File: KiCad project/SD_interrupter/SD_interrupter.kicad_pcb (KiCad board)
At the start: 2 copper layers, 83.8 x 86.4 mm, 36 parts, among them J1 Micro_SD_Card_Det, J2 AVR-ISP-6, J3 DIN-5, SW1 BL_SW, SW2 MAIN_SW, SW3 UP_SW, SW4 DN_SW, SW5 OK_SW, U1 LM7805_TO220, U2 4050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

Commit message: minor changes
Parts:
- added J4: Jack-DC, Connector_BarrelJack:BarrelJack_Horizontal, F.Cu at (90.7, 86.9)
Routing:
- net VCC: track 29.1 -> 95.3 mm
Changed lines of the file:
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@@
   (net 23 "unconnected-(J1-Pad1)")
   (net 24 "Net-(J1-Pad2)")
-  (net 25 "Net-(U2-Pad4)")
+  (net 25 "Net-(J1-Pad3)")
   (net 26 "Net-(J1-Pad5)")
   (net 27 "/DO")
@@
       (net 31 "/CLK") (pintype "input"))
     (pad "4" thru_hole oval (at 0 7.62 180) (size 1.6 1.6) (drill 0.8) (layers *.Cu *.Mask)
-      (net 25 "Net-(U2-Pad4)") (pintype "output"))
+      (net 25 "Net-(J1-Pad3)") (pintype "output"))
     (pad "5" thru_hole oval (at 0 10.16 180) (size 1.6 1.6) (drill 0.8) (layers *.Cu *.Mask)
       (net 32 "/DI") (pintype "input"))
@@
     (fp_circle (center 3.25 2.25) (end 1.25 2.5) (layer "F.Fab") (width 0.1) (fill none))
     (pad "1" thru_hole circle (at 0 0 90) (size 2 2) (drill 1.1) (layers *.Cu *.Mask)
-      (net 3 "GND") (pinfunction "2") (pintype "passive"))
+      (net 3 "GND") (pinfunction "1") (pintype "passive"))
     (pad "1" thru_hole circle (at 6.5 0 90) (size 2 2) (drill 1.1) (layers *.Cu *.Mask)
-      (net 3 "GND") (pinfunction "2") (pintype "passive"))
+      (net 3 "GND") (pinfunction "1") (pintype "passive"))
     (pad "2" thru_hole circle (at 6.5 4.5 90) (size 2 2) (drill 1.1) (layers *.Cu *.Mask)
       (net 38 "/UP") (pinfunction "A") (pintype "passive"))
@@
       (net 33 "/RESET") (pintype "passive"))
     (model "${KICAD6_3DMODEL_DIR}/Resistor_THT.3dshapes/R_Axial_DIN0204_L3.6mm_D1.6mm_P7.62mm_Horizontal.wrl"
+      (offset (xyz 0 0 0))
+      (scale (xyz 1 1 1))
+      (rotate (xyz 0 0 0))
+    )
+  )
+  (footprint "Connector_BarrelJack:BarrelJack_Horizontal" (layer "F.Cu")
+    (at 90.678 86.868 180)
+    (descr "DC Barrel Jack")
+    (tags "Power Jack")
+    (property "Sheetfile" "SD_interrupter.kicad_sch")
+    (property "Sheetname" "")
+    (attr through_hole)
+    (fp_text reference "J4" (at -8.45 5.75) (layer "F.SilkS")
+      (effects (font (size 1 1) (thickness 0.15)))
+    )
+    (fp_text value "Jack-DC" (at -6.2 -5.5) (layer "F.Fab")
+      (effects (font (size 1 1) (thickness 0.15)))
+    )
+    (fp_text user "${REFERENCE}" (at -3 -2.95) (layer "F.Fab")
+      (effects (font (size 1 1) (thickness 0.15)))
+    )
+    (fp_line (start -13.8 -4.6) (end 0.9 -4.6) (layer "F.SilkS") (width 0.12))
+    (fp_line (start -13.8 4.6) (end -13.8 -4.6) (layer "F.SilkS") (width 0.12))
+    (fp_line (start 0.9 1.9) (end 0.9 4.6) (layer "F.SilkS") (width 0.12))
+    (fp_line (start 0.05 -4.8) (end 1.1 -4.8) (layer "F.SilkS") (width 0.12))
+    (fp_line (start -5 4.6) (end -13.8 4.6) (layer "F.SilkS") (width 0.12))
+    (fp_line (start 0.9 -4.6) (end 0.9 -2) (layer "F.SilkS") (width 0.12))
+    (fp_line (start 0.9 4.6) (end -1 4.6) (layer "F.SilkS") (width 0.12))
+    (fp_line (start 1.1 -3.75) (end 1.1 -4.8) (layer "F.SilkS") (width 0.12))
+    (fp_line (start 2 -2) (end 2 2) (layer "F.CrtYd") (width 0.05))
+    (fp_line (start 2 2) (end 1 2) (layer "F.CrtYd") (width 0.05))
+    (fp_line (start -14 4.75) (end -14 -4.75) (layer "F.CrtYd") (width 0.05))
+    (fp_line (start 1 4.75) (end -1 4.75) (layer "F.CrtYd") (width 0.05))
+    (fp_line (start 1 2) (end 1 4.75) (layer "F.CrtYd") (width 0.05))
+    (fp_line (start 1 -4.5) (end 1 -2) (layer "F.CrtYd") (width 0.05))
+    (fp_line (start 1 -4.75) (end -14 -4.75) (layer "F.CrtYd") (width 0.05))
+    (fp_line (start 1 -2) (end 2 -2) (layer "F.CrtYd") (width 0.05))
+    (fp_line (start -1 6.75) (end -5 6.75) (layer "F.CrtYd") (width 0.05))
+    (fp_line (start -5 6.75) (end -5 4.75) (layer "F.CrtYd") (width 0.05))
+    (fp_line (start -1 4.75) (end -1 6.75) (layer "F.CrtYd") (width 0.05))
+    (fp_line (start 1 -4.5) (end 1 -4.75) (layer "F.CrtYd") (width 0.05))
+    (fp_line (start -5 4.75) (end -14 4.75) (layer "F.CrtYd") (width 0.05))
+    (fp_line (start -13.7 4.5) (end 0.8 4.5) (layer "F.Fab") (width 0.1))
+    (fp_line (start 0.8 4.5) (end 0.8 -3.75) (layer "F.Fab") (width 0.1))
+    (fp_line (start 0 -4.5) (end -13.7 -4.5) (layer "F.Fab") (width 0.1))
+    (fp_line (start -10.2 -4.5) (end -10.2 4.5) (layer "F.Fab") (width 0.1))
+    (fp_line (start -13.7 -4.5) (end -13.7 4.5) (layer "F.Fab") (width 0.1))
+    (fp_line (start -0.003213 -4.505425) (end 0.8 -3.75) (layer "F.Fab") (width 0.1))
+    (pad "1" thru_hole rect (at 0 0 180) (size 3.5 3.5) (drill oval 1 3) (layers *.Cu *.Mask)
+      (net 2 "VCC") (pintype "passive"))
+    (pad "2" thru_hole roundrect (at -6 0 180) (size 3 3.5) (drill oval 1 3) (layers *.Cu *.Mask) (roundrect_rratio 0.25)
+      (net 3 "GND") (pintype "passive"))
+    (pad "3" thru_hole roundrect (at -3 4.7 180) (size 3.5 3.5) (drill oval 3 1) (layers *.Cu *.Mask) (roundrect_rratio 0.25))
+    (model "${KICAD6_3DMODEL_DIR}/Connector_BarrelJack.3dshapes/BarrelJack_Horizontal.wrl"
       (offset (xyz 0 0 0))
       (scale (xyz 1 1 1))
@@
     (fp_circle (center 3.25 2.25) (end 1.25 2.5) (layer "F.Fab") (width 0.1) (fill none))
     (pad "1" thru_hole circle (at 6.5 0 90) (size 2 2) (drill 1.1) (layers *.Cu *.Mask)
-      (net 3 "GND") (pinfunction "1") (pintype "passive"))
+      (net 3 "GND") (pinfunction "2") (pintype "passive"))
     (pad "1" thru_hole circle (at 0 0 90) (size 2 2) (drill 1.1) (layers *.Cu *.Mask)
-      (net 3 "GND") (pinfunction "1") (pintype "passive"))
+      (net 3 "GND") (pinfunction "2") (pintype "passive"))
     (pad "2" thru_hole circle (at 0 4.5 90) (size 2 2) (drill 1.1) (layers *.Cu *.Mask)
       (net 39 "/DN") (pinfunction "A") (pintype "passive"))
@@
       (net 24 "Net-(J1-Pad2)") (pinfunction "DAT3/CD") (pintype "bidirectional"))
     (pad "3" smd rect (at 0.575 -7.725 90) (size 0.7 1.2) (layers "F.Cu" "F.Paste" "F.Mask")
-      (net 25 "Net-(U2-Pad4)") (pinfunction "CMD") (pintype "input"))
+      (net 25 "Net-(J1-Pad3)") (pinfunction "CMD") (pintype "input"))
     (pad "4" smd rect (at -0.525 -7.725 90) (size 0.7 1.2) (layers "F.Cu" "F.Paste" "F.Mask")
       (net 6 "+3.3V") (pinfunction "VDD") (pintype "power_in"))
@@
     (fp_circle (center 3.25 2.25) (end 1.25 2.5) (layer "F.Fab") (width 0.1) (fill none))
     (pad "1" thru_hole circle (at 0 0 90) (size 2 2) (drill 1.1) (layers *.Cu *.Mask)
-      (net 3 "GND") (pinfunction "1") (pintype "passive"))
+      (net 3 "GND") (pinfunction "2") (pintype "passive"))
     (pad "1" thru_hole circle (at 6.5 0 90) (size 2 2) (drill 1.1) (layers *.Cu *.Mask)
-      (net 3 "GND") (pinfunction "1") (pintype "passive"))
+      (net 3 "GND") (pinfunction "2") (pintype "passive"))
     (pad "2" thru_hole circle (at 0 4.5 90) (size 2 2) (drill 1.1) (layers *.Cu *.Mask)
       (net 40 "/OK") (pinfunction "A") (pintype "passive"))
@@
     (fp_line (start 68 28) (end -5 28) (layer "F.SilkS") (width 0.12))
     (fp_line (start -8.14 -2.64) (end -8.14 33.64) (layer "F.SilkS") (width 0.12))
-    (fp_arc (start 64.20104 22.49932) (mid 64.054473 22.853115) (end 63.70066 22.9997) (layer "F.SilkS") (width 0.12))
+    (fp_arc (start 64.20104 22.49932) (mid 64.054479 22.85315) (end 63.70066 22.9997) (layer "F.SilkS") (width 0.12))
     (fp_arc (start 0.20066 22.9997) (mid -0.153162 22.853142) (end -0.29972 22.49932) (layer "F.SilkS") (width 0.12))
     (fp_arc (start 63.7 8) (mid 64.053553 8.146447) (end 64.2 8.5) (layer "F.SilkS") (width 0.12))
@@
   (segment (start 48.561315 106.981315) (end 50.165 108.585) (width 0.635) (layer "B.Cu") (net 1))
   (segment (start 30.1445 69.5125) (end 30.1445 49.5755) (width 0.635) (layer "B.Cu") (net 2))
+  (segment (start 71.72907 86.868) (end 69.26357 84.4025) (width 0.635) (layer "B.Cu") (net 2))
+  (segment (start 90.678 86.868) (end 71.72907 86.868) (width 0.635) (layer "B.Cu") (net 2))
   (segment (start 31.247 70.615) (end 30.1445 69.5125) (width 0.635) (layer "B.Cu") (net 2))
   (segment (start 30.1445 49.5755) (end 24.765 44.196) (width 0.635) (layer "B.Cu") (net 2))
+  (segment (start 45.0345 84.4025) (end 31.247 70.615) (width 0.635) (layer "B.Cu") (net 2))
+  (segment (start 69.26357 84.4025) (end 45.0345 84.4025) (width 0.635) (layer "B.Cu") (net 2))
   (segment (start 72.39 31.75) (end 72.39 31.83) (width 0.635) (layer "F.Cu") (net 3))
   (segment (start 72.39 31.83) (end 76.12 35.56) (width 0.635) (layer "F.Cu") (net 3))

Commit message: minor changes
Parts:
- added J5: VCC, Connector_PinSocket_2.54mm:PinSocket_1x02_P2.54mm_Vertical, F.Cu at (25.7, 66.0)
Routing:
- net VCC: track 95.3 -> 102.8 mm
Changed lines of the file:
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@@
       (net 3 "GND") (pinfunction "1") (pintype "passive"))
     (pad "2" thru_hole circle (at 6.5 4.5 90) (size 2 2) (drill 1.1) (layers *.Cu *.Mask)
-      (net 38 "/UP") (pinfunction "A") (pintype "passive"))
+      (net 38 "/UP") (pinfunction "K") (pintype "passive"))
     (pad "2" thru_hole circle (at 0 4.5 90) (size 2 2) (drill 1.1) (layers *.Cu *.Mask)
-      (net 38 "/UP") (pinfunction "A") (pintype "passive"))
+      (net 38 "/UP") (pinfunction "K") (pintype "passive"))
     (model "${KICAD6_3DMODEL_DIR}/Button_Switch_THT.3dshapes/SW_PUSH_6mm_H7.3mm.wrl"
       (offset (xyz 0 0 0))
@@
       (net 5 "+5V") (pinfunction "IN") (pintype "power_in"))
     (model "${KICAD6_3DMODEL_DIR}/Package_TO_SOT_THT.3dshapes/TO-92.wrl"
+      (offset (xyz 0 0 0))
+      (scale (xyz 1 1 1))
+      (rotate (xyz 0 0 0))
+    )
+  )
+  (footprint "Connector_PinSocket_2.54mm:PinSocket_1x02_P2.54mm_Vertical" (layer "F.Cu")
+    (at 25.654 66.04 180)
+    (descr "Through hole straight socket strip, 1x02, 2.54mm pitch, single row (from Kicad 4.0.7), script generated")
+    (tags "Through hole socket strip THT 1x02 2.54mm single row")
+    (property "Sheetfile" "SD_interrupter.kicad_sch")
+    (property "Sheetname" "")
+    (attr through_hole)
+    (fp_text reference "J5" (at 0 -2.77) (layer "F.SilkS")
+      (effects (font (size 1 1) (thickness 0.15)))
+    )
+    (fp_text value "VCC" (at 0 5.31) (layer "F.Fab")
+      (effects (font (size 1 1) (thickness 0.15)))
+    )
+    (fp_text user "${REFERENCE}" (at 0 1.27 90) (layer "F.Fab")
+      (effects (font (size 1 1) (thickness 0.15)))
+    )
+    (fp_line (start -1.33 3.87) (end 1.33 3.87) (layer "F.SilkS") (width 0.12))
+    (fp_line (start 0 -1.33) (end 1.33 -1.33) (layer "F.SilkS") (width 0.12))
+    (fp_line (start 1.33 1.27) (end 1.33 3.87) (layer "F.SilkS") (width 0.12))
+    (fp_line (start -1.33 1.27) (end -1.33 3.87) (layer "F.SilkS") (width 0.12))
+    (fp_line (start -1.33 1.27) (end 1.33 1.27) (layer "F.SilkS") (width 0.12))
+    (fp_line (start 1.33 -1.33) (end 1.33 0) (layer "F.SilkS") (width 0.12))
+    (fp_line (start 1.75 -1.8) (end 1.75 4.3) (layer "F.CrtYd") (width 0.05))
+    (fp_line (start -1.8 -1.8) (end 1.75 -1.8) (layer "F.CrtYd") (width 0.05))
+    (fp_line (start 1.75 4.3) (end -1.8 4.3) (layer "F.CrtYd") (width 0.05))
+    (fp_line (start -1.8 4.3) (end -1.8 -1.8) (layer "F.CrtYd") (width 0.05))
+    (fp_line (start -1.27 3.81) (end -1.27 -1.27) (layer "F.Fab") (width 0.1))
+    (fp_line (start -1.27 -1.27) (end 0.635 -1.27) (layer "F.Fab") (width 0.1))
+    (fp_line (start 0.635 -1.27) (end 1.27 -0.635) (layer "F.Fab") (width 0.1))
+    (fp_line (start 1.27 -0.635) (end 1.27 3.81) (layer "F.Fab") (width 0.1))
+    (fp_line (start 1.27 3.81) (end -1.27 3.81) (layer "F.Fab") (width 0.1))
+    (pad "1" thru_hole rect (at 0 0 180) (size 1.7 1.7) (drill 1) (layers *.Cu *.Mask)
+      (net 2 "VCC") (pinfunction "Pin_1") (pintype "passive"))
+    (pad "2" thru_hole oval (at 0 2.54 180) (size 1.7 1.7) (drill 1) (layers *.Cu *.Mask)
+      (net 3 "GND") (pinfunction "Pin_2") (pintype "passive"))
+    (model "${KICAD6_3DMODEL_DIR}/Connector_PinSocket_2.54mm.3dshapes/PinSocket_1x02_P2.54mm_Vertical.wrl"
       (offset (xyz 0 0 0))
       (scale (xyz 1 1 1))
@@
       (net 3 "GND") (pinfunction "2") (pintype "passive"))
     (pad "2" thru_hole circle (at 0 4.5 90) (size 2 2) (drill 1.1) (layers *.Cu *.Mask)
-      (net 39 "/DN") (pinfunction "A") (pintype "passive"))
+      (net 39 "/DN") (pinfunction "K") (pintype "passive"))
     (pad "2" thru_hole circle (at 6.5 4.5 90) (size 2 2) (drill 1.1) (layers *.Cu *.Mask)
-      (net 39 "/DN") (pinfunction "A") (pintype "passive"))
+      (net 39 "/DN") (pinfunction "K") (pintype "passive"))
     (model "${KICAD6_3DMODEL_DIR}/Button_Switch_THT.3dshapes/SW_PUSH_6mm_H7.3mm.wrl"
       (offset (xyz 0 0 0))
@@
     (fp_circle (center 3.25 2.25) (end 1.25 2.5) (layer "F.Fab") (width 0.1) (fill none))
     (pad "1" thru_hole circle (at 0 0 90) (size 2 2) (drill 1.1) (layers *.Cu *.Mask)
-      (net 3 "GND") (pinfunction "2") (pintype "passive"))
+      (net 3 "GND") (pinfunction "1") (pintype "passive"))
     (pad "1" thru_hole circle (at 6.5 0 90) (size 2 2) (drill 1.1) (layers *.Cu *.Mask)
-      (net 3 "GND") (pinfunction "2") (pintype "passive"))
+      (net 3 "GND") (pinfunction "1") (pintype "passive"))
     (pad "2" thru_hole circle (at 0 4.5 90) (size 2 2) (drill 1.1) (layers *.Cu *.Mask)
       (net 40 "/OK") (pinfunction "A") (pintype "passive"))
@@
     (fp_line (start 68 28) (end -5 28) (layer "F.SilkS") (width 0.12))
     (fp_line (start -8.14 -2.64) (end -8.14 33.64) (layer "F.SilkS") (width 0.12))
-    (fp_arc (start 64.20104 22.49932) (mid 64.054479 22.85315) (end 63.70066 22.9997) (layer "F.SilkS") (width 0.12))
+    (fp_arc (start 64.20104 22.49932) (mid 64.054473 22.853115) (end 63.70066 22.9997) (layer "F.SilkS") (width 0.12))
     (fp_arc (start 0.20066 22.9997) (mid -0.153162 22.853142) (end -0.29972 22.49932) (layer "F.SilkS") (width 0.12))
     (fp_arc (start 63.7 8) (mid 64.053553 8.146447) (end 64.2 8.5) (layer "F.SilkS") (width 0.12))
@@
   (segment (start 31.247 108.585) (end 32.850685 106.981315) (width 0.635) (layer "B.Cu") (net 1))
   (segment (start 48.561315 106.981315) (end 50.165 108.585) (width 0.635) (layer "B.Cu") (net 1))
+  (segment (start 26.672 66.04) (end 31.247 70.615) (width 0.635) (layer "F.Cu") (net 2))
+  (segment (start 25.654 66.04) (end 26.672 66.04) (width 0.635) (layer "F.Cu") (net 2))
   (segment (start 30.1445 69.5125) (end 30.1445 49.5755) (width 0.635) (layer "B.Cu") (net 2))
   (segment (start 71.72907 86.868) (end 69.26357 84.4025) (width 0.635) (layer "B.Cu") (net 2))

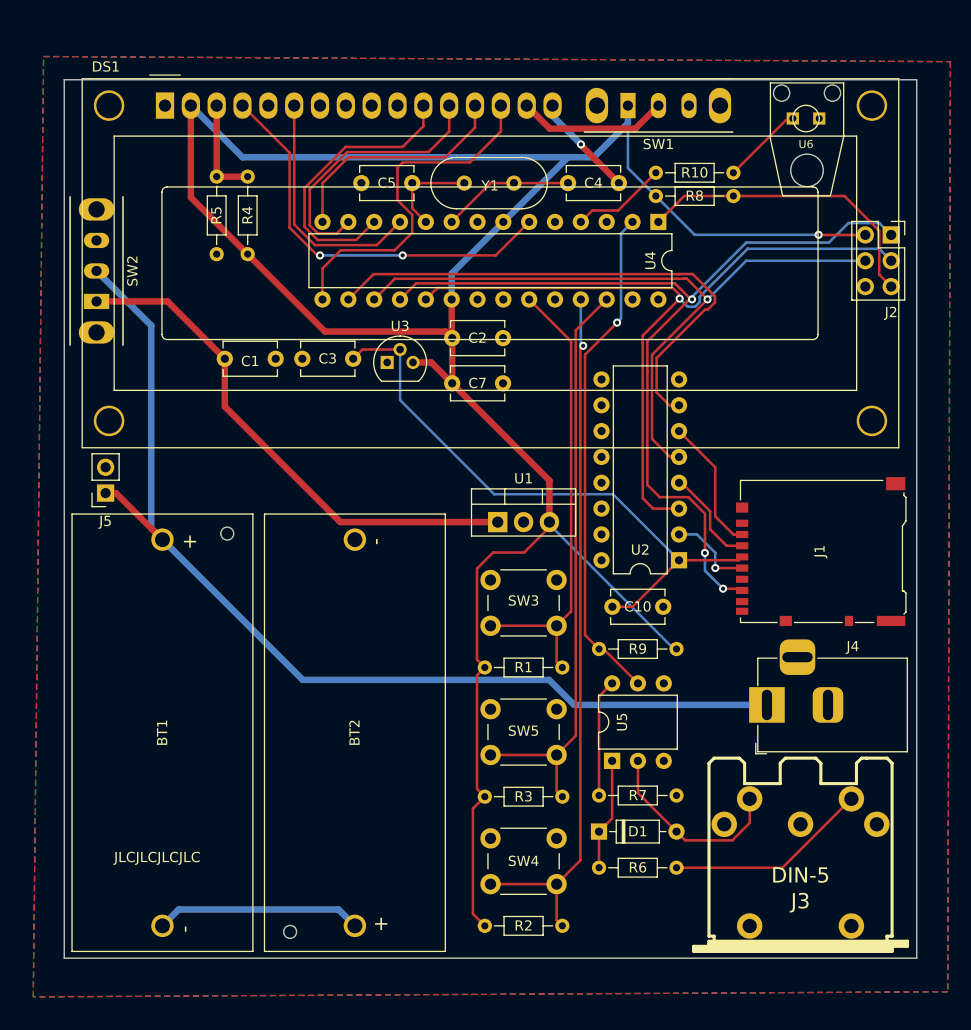
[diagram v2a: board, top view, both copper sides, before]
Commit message: different 3.3V regulator footprint
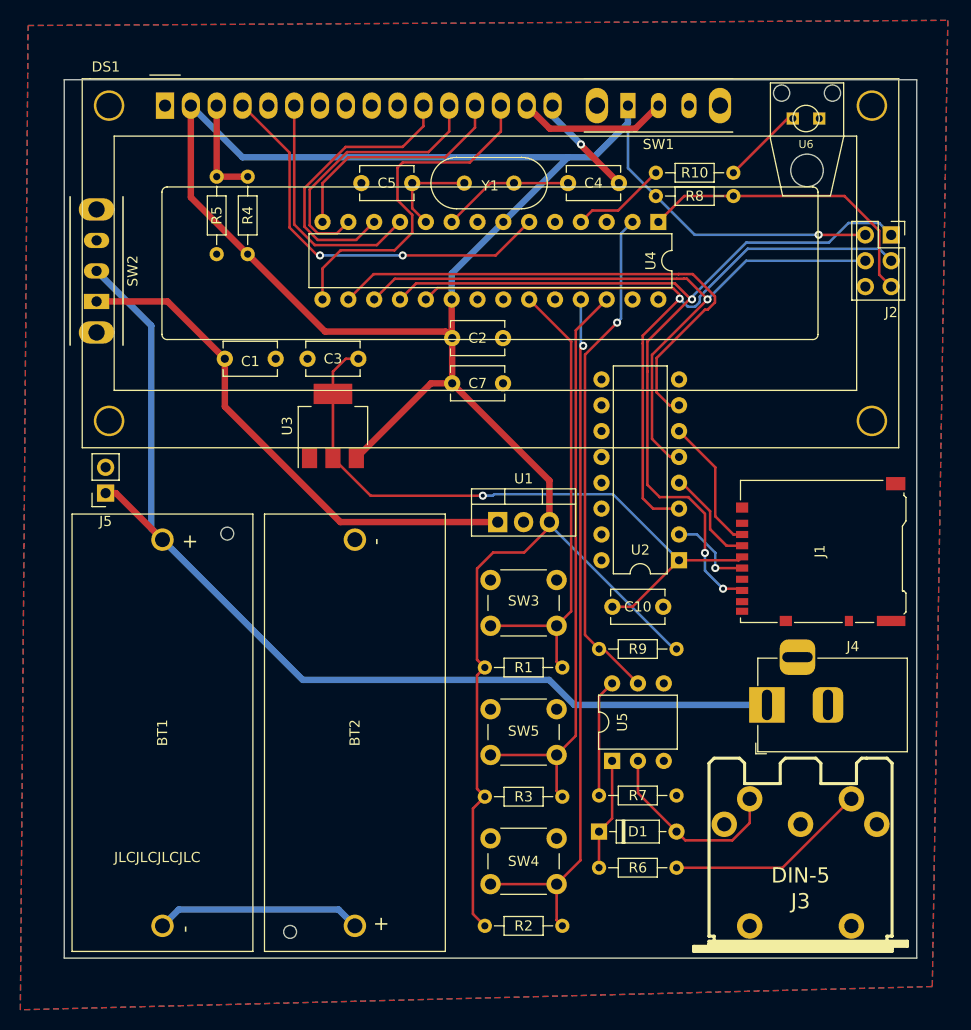
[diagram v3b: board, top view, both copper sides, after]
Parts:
- U3: value LD1086V33-DG -> AMS1117-3.3; footprint Package_TO_SOT_THT:TO-92 -> Package_TO_SOT_SMD:SOT-223-3_TabPin2
- moved U3 8.21 mm to (48.0, 59.4), turned to 90 degrees
- moved C3 0.51 mm to (50.5, 52.8)
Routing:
- net +5V: track 234.4 -> 242.1 mm
- net +3.3V: track 58.7 -> 64.6 mm, vias 0 -> 1

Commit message: gerbers update
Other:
- board text added: "GND"
- board text added: "VCC"
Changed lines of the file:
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@@
     (effects (font (size 1 1) (thickness 0.15)) (justify mirror))
+  )
+  (gr_text "GND" (at 29.718 63.5) (layer "F.SilkS")
+    (effects (font (size 1.5 1.5) (thickness 0.3)))
+  )
+  (gr_text "VCC" (at 29.718 66.294) (layer "F.SilkS")
+    (effects (font (size 1.5 1.5) (thickness 0.3)))
   )
   (gr_text "JLCJLCJLCJLC" (at 30.734 101.854) (layer "F.SilkS")

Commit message: safety switch
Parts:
- added SW6: BL_SW, Switch:Switch 12x6mm, F.Cu at (102.1, 39.6)
- moved J2 9.39 mm to (103.1, 50.0)
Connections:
- U6 pad P$2: /OPT -> Net-(U6-PadP$2)
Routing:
- net Net-(U6-PadP$2): track 0.00 -> 14.1 mm
- net /OPT: track 8.05 -> 18.1 mm
- net +5V: track 242.1 -> 246.2 mm, vias 1 -> 0
- net /RESET: track 30.2 -> 33.9 mm
- net /DI: track 70.9 -> 72.0 mm
